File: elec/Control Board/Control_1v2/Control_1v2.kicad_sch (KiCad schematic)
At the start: 164 parts, among them J1 DB9_Female_MountingHoles, J10 Conn_02x12_Odd_Even, J11 Screw_Terminal_01x02, J14 Conn_01x10, J2 Conn_01x08, J25 Screw_Terminal_01x02, J26 Conn_01x10, J27 Conn_02x12_Odd_Even, J28 Screw_Terminal_01x02, J29 Conn_01x10, J3 Conn_01x08, J37 Conn_01x04, J4 Conn_01x08, J5 Conn_01x08, J6 Conn_01x08, J7 Conn_01x10, J8 Conn_02x18_Odd_Even, J9 Conn_01x10, Q601 BSS138

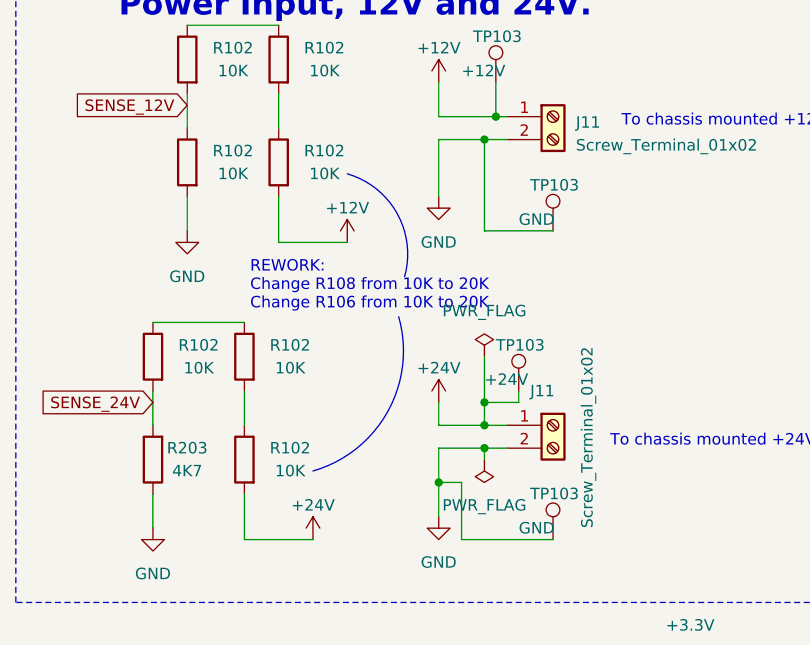
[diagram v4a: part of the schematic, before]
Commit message: Contrl 1.2 schematic, fix for Issue: not enough overhead on the 12v and 24v sense lines #145
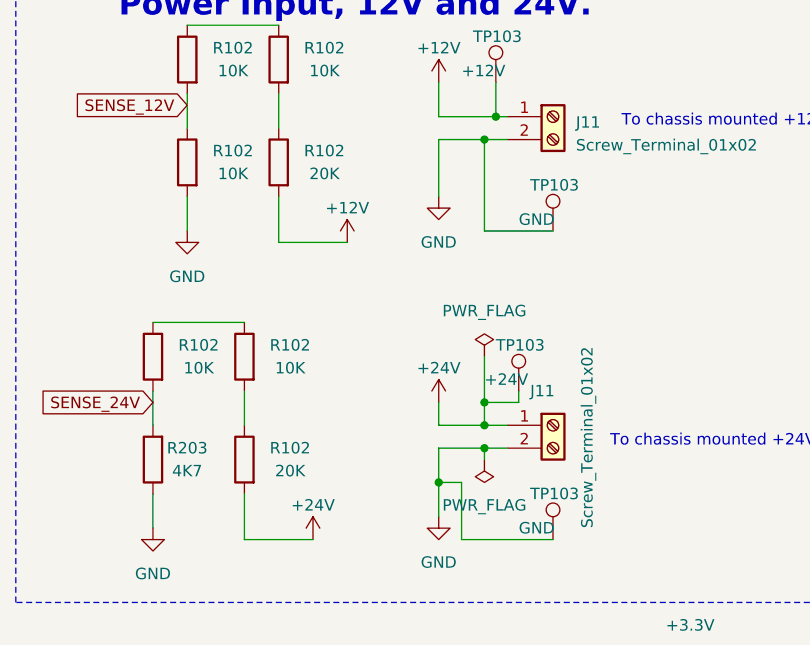
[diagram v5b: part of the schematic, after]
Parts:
- R102: value 10K -> 20K; Cost 0.0015 -> 0.0008; Distributor 1 PN C269701 -> C25804; MPN RMC060310KFN -> 0603WAF1002T5E; Manufacturer TyoHM -> UNI-ROYAL(Uniroyal Elec)
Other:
- note removed: "REWORK: Change R108 from 10K to 20K Change R106 from 10K to 20K"
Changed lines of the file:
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@@
     (stroke (width 0) (type default))
   )
-  (arc (start 459.74 178.435) (mid 465.2823 182.8401) (end 466.108 189.875)
-    (stroke (width 0) (type default))
-    (fill (type none))
-  )
   (rectangle (start 160.02 211.455) (end 259.715 272.415)
     (stroke (width 0.0762) (type dash))
@@
     (fill (type none))
   )
-  (arc (start 465.455 194.31) (mid 464.2381 204.8523) (end 455.93 211.455)
-    (stroke (width 0) (type default))
-    (fill (type none))
-  )
   (image (at 508 294.64) (scale 0.75)
     (data
@@
     (effects (font (size 1.27 1.27)) (justify left bottom))
   )
-  (text "REWORK:\nChange R108 from 10K to 20K\nChange R106 from 10K to 20K"
-    (at 448.945 193.675 0)
-    (effects (font (size 1.27 1.27)) (justify left bottom))
-  )
   (text "One Wire Thermocouple amplifiter\nDATA is bidirectional GPIO"
     (at 61.595 161.925 0)
@@
       (effects (font (size 1.27 1.27)))
     )
-    (property "Value" "10K" (at 453.39 211.455 0)
+    (property "Value" "20K" (at 453.39 211.455 0)
       (effects (font (size 1.27 1.27)))
     )
@@
       (effects (font (size 1.27 1.27)) hide)
     )
-    (property "Distributor 1 PN" "C269701" (at 448.31 210.185 90)
+    (property "Distributor 1 PN" "C25804" (at 448.31 210.185 90)
       (effects (font (size 1.27 1.27)) hide)
     )
-    (property "Manufacturer" "TyoHM" (at 448.31 210.185 90)
+    (property "Manufacturer" "UNI-ROYAL(Uniroyal Elec)" (at 448.31 210.185 90)
       (effects (font (size 1.27 1.27)) hide)
     )
-    (property "MPN" "RMC060310KFN" (at 448.31 210.185 90)
+    (property "MPN" "0603WAF1002T5E" (at 448.31 210.185 90)
       (effects (font (size 1.27 1.27)) hide)
     )
-    (property "Description" "100mW ±1% 10kΩ 0603 Chip Resistor - Surface Mount ROHS" (at 448.31 210.185 0)
+    (property "Description" "100mW Thick Film Resistors 75V ±100ppm/℃ ±1% 10kΩ 0603 Chip Resistor - Surface Mount ROHS" (at 448.31 210.185 0)
       (effects (font (size 1.27 1.27)) hide)
     )
@@
       (effects (font (size 1.27 1.27)) hide)
     )
-    (property "Cost" "0.0015" (at 448.31 210.185 0)
+    (property "Cost" "0.0008" (at 448.31 210.185 0)
       (effects (font (size 1.27 1.27)) hide)
     )
@@
       (effects (font (size 1.27 1.27)))
     )
-    (property "Value" "10K" (at 457.2 178.435 0)
+    (property "Value" "20K" (at 457.2 178.435 0)
       (effects (font (size 1.27 1.27)))
     )
@@
       (effects (font (size 1.27 1.27)) hide)
     )
-    (property "Distributor 1 PN" "C269701" (at 452.12 177.165 90)
+    (property "Distributor 1 PN" "C25804" (at 452.12 177.165 90)
       (effects (font (size 1.27 1.27)) hide)
     )
-    (property "Manufacturer" "TyoHM" (at 452.12 177.165 90)
+    (property "Manufacturer" "UNI-ROYAL(Uniroyal Elec)" (at 452.12 177.165 90)
       (effects (font (size 1.27 1.27)) hide)
     )
-    (property "MPN" "RMC060310KFN" (at 452.12 177.165 90)
+    (property "MPN" "0603WAF1002T5E" (at 452.12 177.165 90)
       (effects (font (size 1.27 1.27)) hide)
     )
-    (property "Description" "100mW ±1% 10kΩ 0603 Chip Resistor - Surface Mount ROHS" (at 452.12 177.165 0)
+    (property "Description" "100mW Thick Film Resistors 75V ±100ppm/℃ ±1% 10kΩ 0603 Chip Resistor - Surface Mount ROHS" (at 452.12 177.165 0)
       (effects (font (size 1.27 1.27)) hide)
     )
@@
       (effects (font (size 1.27 1.27)) hide)
     )
-    (property "Cost" "0.0015" (at 452.12 177.165 0)
+    (property "Cost" "0.0008" (at 452.12 177.165 0)
       (effects (font (size 1.27 1.27)) hide)
     )

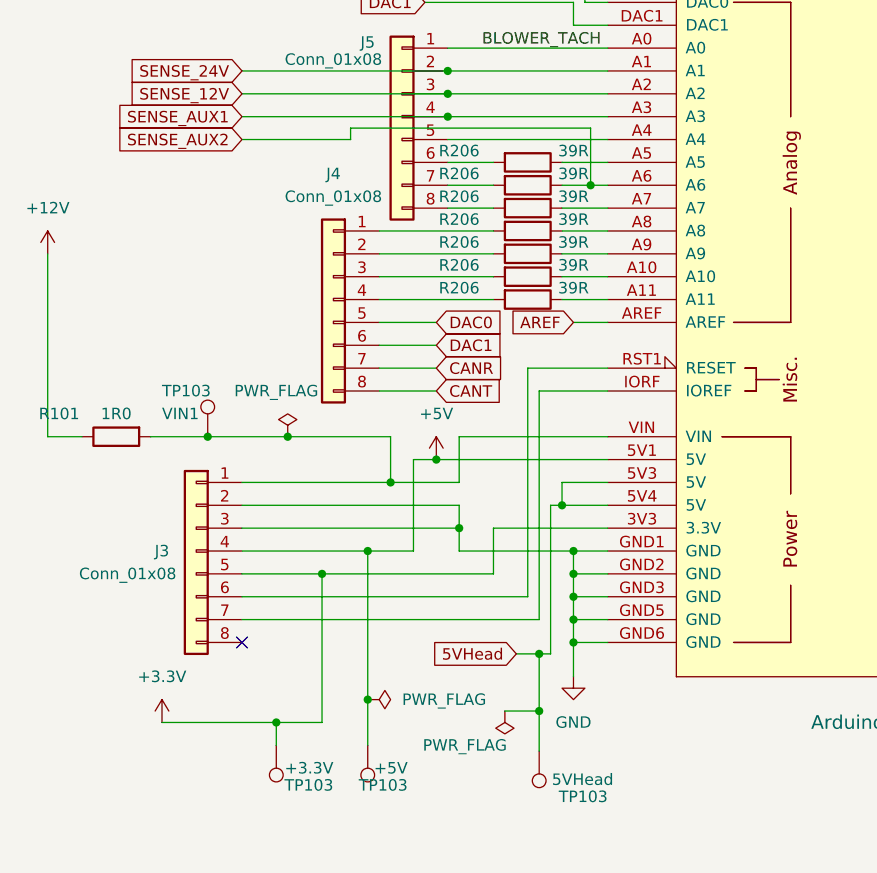
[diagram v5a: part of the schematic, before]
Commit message: Contrl 1.2 schematic, fix for Issue: Connect J3 pin 8 to the Due, Footrpint Arduino_Due_Shield_Annotated Missing Pin Number on ND on Schematic symbol and footprint. #348
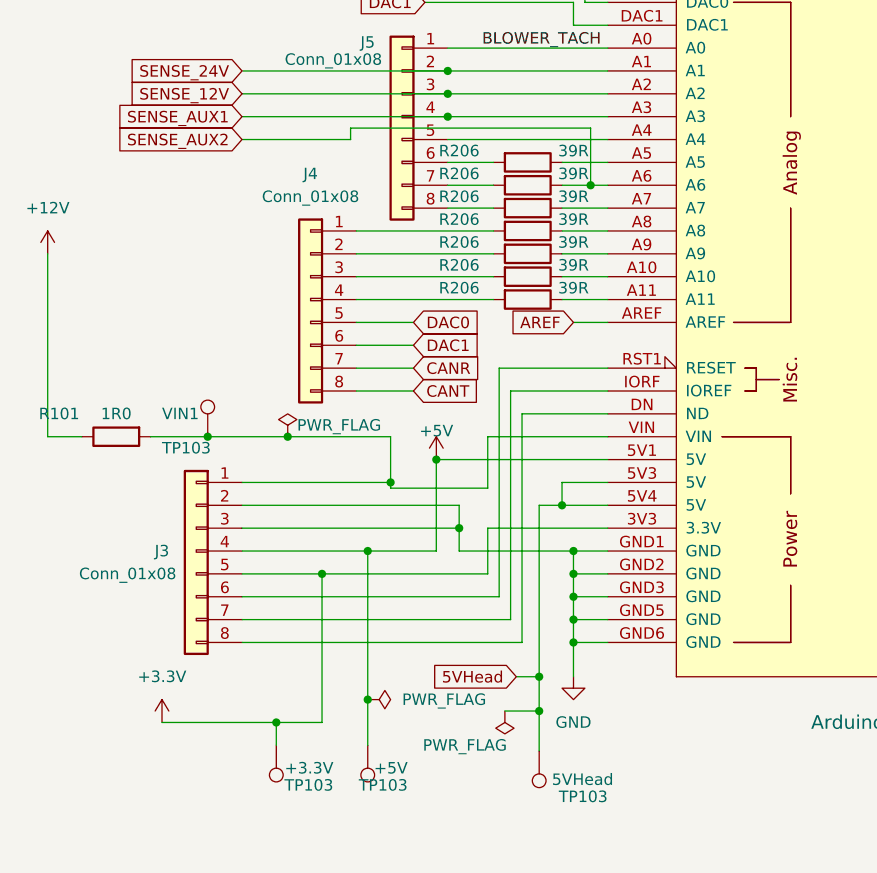
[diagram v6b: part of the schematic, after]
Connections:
- net at J3.8 (Pin_8): now also A1.DN (ND)
- no-connect marks 3 -> 2
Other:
- moved on the sheet: J4

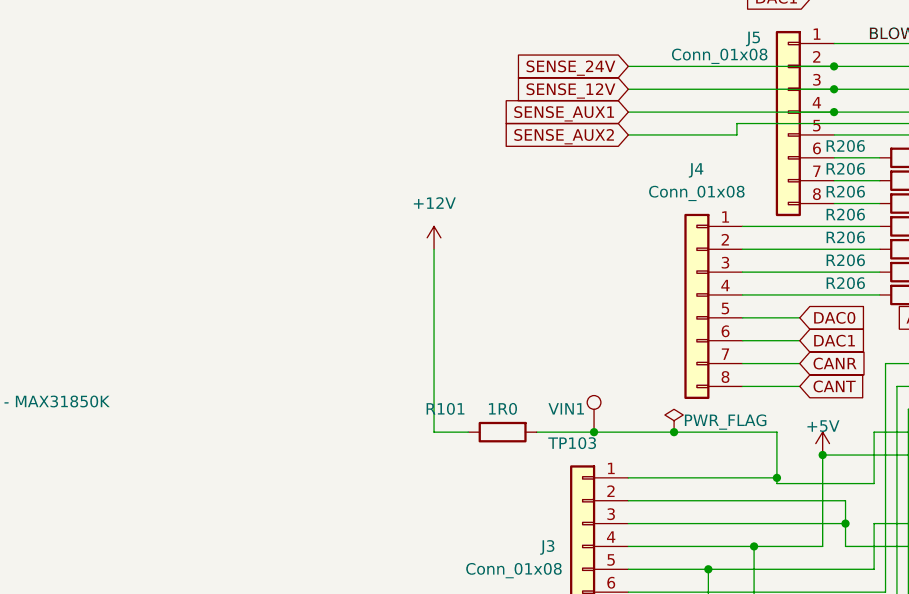
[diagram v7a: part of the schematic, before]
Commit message: Update Control_1v2.kicad_sch for Add Assembly versioning resistors #350.
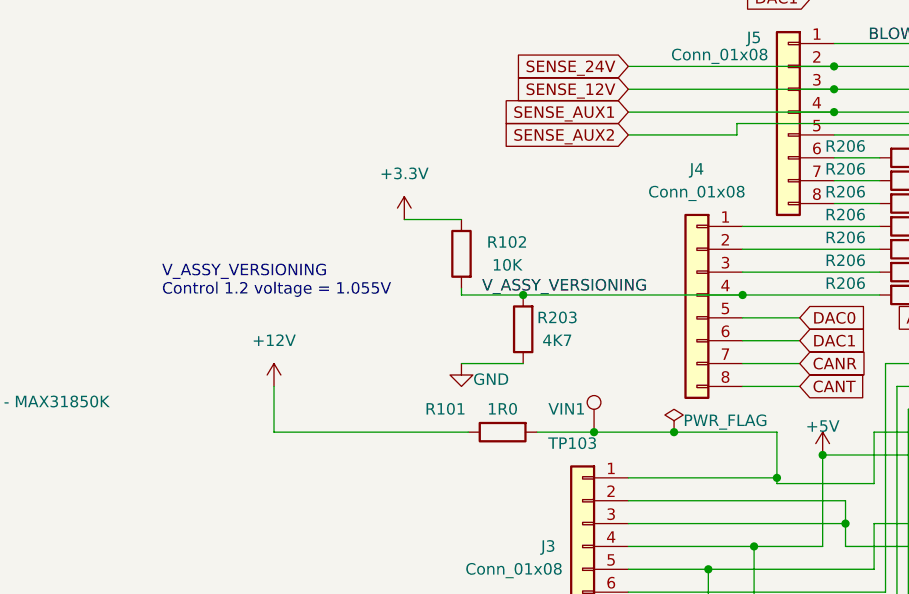
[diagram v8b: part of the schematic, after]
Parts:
- added R102: 10K, Resistor_SMD:R_0603_1608Metric_Pad0.98x0.95mm_HandSolder, symbol Device:R
- added R203: 4K7, Resistor_SMD:R_0603_1608Metric_Pad0.98x0.95mm_HandSolder, symbol Device:R
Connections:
- net +3.3V: now also R102.1
- net GND: now also R203.1
- net V_ASSY_VERSIONING: now reaches J4.4 (Pin_4), R206.2
- net V_ASSY_VERSIONING: now also R102.2, R203.2
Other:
- note added: "V_ASSY_VERSIONING Control 1.2 voltage = 1.055V"
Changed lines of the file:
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@@
   (junction (at 214.63 234.95) (diameter 0) (color 0 0 0 0)
   )
+  (junction (at 164.846 137.16) (diameter 0) (color 0 0 0 0)
+  )
   (junction (at 269.24 204.47) (diameter 0) (color 0 0 0 0)
   )
@@
   (junction (at 64.77 44.45) (diameter 0) (color 0 0 0 0)
   )
+  (junction (at 189.23 137.16) (diameter 0) (color 0 0 0 0)
+  )
   (junction (at 213.36 175.26) (diameter 0) (color 0 0 0 0)
   )
@@
     (stroke (width 0) (type default))
   )
+  (wire (pts (xy 164.846 137.16) (xy 189.23 137.16))
+    (stroke (width 0) (type default))
+  )
   (wire (pts (xy 443.23 60.96) (xy 433.07 60.96))
     (stroke (width 0) (type default))
@@
     (stroke (width 0) (type default))
   )
+  (wire (pts (xy 151.638 128.778) (xy 157.988 128.778))
+    (stroke (width 0) (type default))
+  )
   (wire (pts (xy 203.2 49.53) (xy 203.2 46.99))
     (stroke (width 0) (type default))
@@
     (stroke (width 0) (type default))
   )
+  (wire (pts (xy 189.23 137.16) (xy 204.47 137.16))
+    (stroke (width 0) (type default))
+  )
   (wire (pts (xy 172.72 152.4) (xy 181.61 152.4))
     (stroke (width 0) (type default))
@@
     (stroke (width 0) (type default))
   )
+  (wire (pts (xy 157.988 137.16) (xy 164.846 137.16))
+    (stroke (width 0) (type default))
+  )
   (wire (pts (xy 273.05 199.39) (xy 269.24 199.39))
     (stroke (width 0) (type default))
@@
     (stroke (width 0) (type default))
   )
+  (wire (pts (xy 157.988 136.398) (xy 157.988 137.16))
+    (stroke (width 0) (type default))
+  )
   (wire (pts (xy 359.41 162.56) (xy 359.41 175.26))
     (stroke (width 0) (type default))
@@
     (stroke (width 0) (type default))
   )
-  (wire (pts (xy 189.23 137.16) (xy 204.47 137.16))
-    (stroke (width 0) (type default))
-  )
   (wire (pts (xy 203.2 46.99) (xy 215.9 46.99))
     (stroke (width 0) (type default))
@@
     (stroke (width 0) (type default))
   )
+  (wire (pts (xy 157.988 144.78) (xy 164.846 144.78))
+    (stroke (width 0) (type default))
+  )
   (wire (pts (xy 477.52 58.42) (xy 455.93 58.42))
     (stroke (width 0) (type default))
@@
     (stroke (width 0) (type default))
   )
-  (wire (pts (xy 154.94 132.08) (xy 154.94 152.4))
+  (wire (pts (xy 137.16 147.32) (xy 137.16 152.4))
     (stroke (width 0) (type default))
   )
@@
     (stroke (width 0) (type default))
   )
-  (wire (pts (xy 154.94 152.4) (xy 158.75 152.4))
+  (wire (pts (xy 137.16 152.4) (xy 158.75 152.4))
     (stroke (width 0) (type default))
   )
@@
     (effects (font (size 2.54 2.54)) (justify left bottom))
   )
+  (text "V_ASSY_VERSIONING\nControl 1.2 voltage = 1.055V" (at 124.714 137.414 0)
+    (effects (font (size 1.27 1.27)) (justify left bottom))
+  )
   (text "Heart beat, \nLoop OK" (at 364.49 87.63 0)
     (effects (font (size 1.27 1.27)) (justify left bottom))
@@
     (effects (font (size 1.27 1.27)) (justify right bottom))
   )
+  (label "V_ASSY_VERSIONING" (at 160.274 137.16 0) (fields_autoplaced)
+    (effects (font (size 1.27 1.27)) (justify left bottom))
+  )
   (label "GND" (at 439.42 66.04 180) (fields_autoplaced)
     (effects (font (size 1.27 1.27)) (justify right bottom))
@@
     )
   )
+  (symbol (lib_id "power:+3.3V") (at 151.638 128.778 0) (mirror y) (unit 1)
+    (in_bom yes) (on_board yes) (dnp no) (fields_autoplaced)
+    (property "Reference" "#PWR064" (at 151.638 132.588 0)
+      (effects (font (size 1.27 1.27)) hide)
+    )
+    (property "Value" "+3.3V" (at 151.638 123.698 0)
+      (effects (font (size 1.27 1.27)))
+    )
+    (property "Footprint" "" (at 151.638 128.778 0)
+      (effects (font (size 1.27 1.27)) hide)
+    )
+    (property "Datasheet" "" (at 151.638 128.778 0)
+      (effects (font (size 1.27 1.27)) hide)
+    )
+    (pin "1")
+    (instances
+      (project "Control_1v2"
+        (path "/c68c9deb-8d4d-42f0-adf8-4d3022f4ee59"
+          (reference "#PWR064") (unit 1)
+        )
+      )
+    )
+  )
   (symbol (lib_id "Device:R") (at 444.5 246.38 270) (unit 1)
     (in_bom yes) (on_board yes) (dnp no)
@@
     )
   )
+  (symbol (lib_id "Device:R") (at 164.846 140.97 180) (unit 1)
+    (in_bom yes) (on_board yes) (dnp no)
+    (property "Reference" "R203" (at 168.656 139.7 0)
+      (effects (font (size 1.27 1.27)))
+    )
+    (property "Value" "4K7" (at 168.656 142.24 0)
+      (effects (font (size 1.27 1.27)))
+    )
+    (property "Footprint" "Resistor_SMD:R_0603_1608Metric_Pad0.98x0.95mm_HandSolder" (at 166.624 140.97 90)
+      (effects (font (size 1.27 1.27)) hide)
+    )
+    (property "Datasheet" "~" (at 164.846 140.97 0)
+      (effects (font (size 1.27 1.27)) hide)
+    )
+    (property "Distributor 1" "JLCPCB" (at 164.846 140.97 90)
+      (effects (font (size 1.27 1.27)) hide)
+    )
+    (property "Distributor 1 PN" "C23162" (at 164.846 140.97 90)
+      (effects (font (size 1.27 1.27)) hide)
+    )
+    (property "Manufacturer" "UNI-ROYAL(Uniroyal Elec)" (at 164.846 140.97 90)
+      (effects (font (size 1.27 1.27)) hide)
+    )
+    (property "MPN" "RMC 0603 4K7 F N" (at 164.846 140.97 90)
+      (effects (font (size 1.27 1.27)) hide)
+    )
+    (property "Description" "100mW Thick Film Resistors ±100ppm/℃ ±1% 4.7kΩ 0603 Chip Resistor - Surface Mount ROHS" (at 164.846 140.97 0)
+      (effects (font (size 1.27 1.27)) hide)
+    )
+    (property "AssemblyType" "SMT" (at 164.846 140.97 0)
+      (effects (font (size 1.27 1.27)) hide)
+    )
+    (property "Cost" "0.0015" (at 164.846 140.97 0)
+      (effects (font (size 1.27 1.27)) hide)
+    )
+    (pin "1")
+    (pin "2")
+    (instances
+      (project "GeneralPurposeAlarmDevicePCB"
+        (path "/412a327d-1ee3-473e-bc00-1545004b7edf/00000000-0000-0000-0000-000062b3ac2f"
+          (reference "R203") (unit 1)
+        )
+      )
+      (project "Control_1v2"
+        (path "/c68c9deb-8d4d-42f0-adf8-4d3022f4ee59"
+          (reference "R?") (unit 1)
+        )
+      )
+    )
+  )
   (symbol (lib_id "Device:R") (at 497.84 256.54 270) (unit 1)
     (in_bom yes) (on_board yes) (dnp no)
@@
     )
   )
-  (symbol (lib_id "power:+12V") (at 154.94 132.08 0) (unit 1)
+  (symbol (lib_id "power:+12V") (at 137.16 147.32 0) (unit 1)
     (in_bom yes) (on_board yes) (dnp no)
-    (property "Reference" "#PWR014" (at 154.94 135.89 0)
+    (property "Reference" "#PWR014" (at 137.16 151.13 0)
       (effects (font (size 1.27 1.27)) hide)
     )
-    (property "Value" "+12V" (at 154.94 127 0)
+    (property "Value" "+12V" (at 137.16 142.24 0)
       (effects (font (size 1.27 1.27)))
     )
-    (property "Footprint" "" (at 154.94 132.08 0)
+    (property "Footprint" "" (at 137.16 147.32 0)
       (effects (font (size 1.27 1.27)) hide)
     )
-    (property "Datasheet" "" (at 154.94 132.08 0)
+    (property "Datasheet" "" (at 137.16 147.32 0)
       (effects (font (size 1.27 1.27)) hide)
     )
@@
     )
   )
+  (symbol (lib_id "power:GND") (at 157.988 144.78 0) (unit 1)
+    (in_bom yes) (on_board yes) (dnp no)
+    (property "Reference" "#PWR0108" (at 157.988 151.13 0)
+      (effects (font (size 1.27 1.27)) hide)
+    )
+    (property "Value" "GND" (at 161.29 146.558 0)
+      (effects (font (size 1.27 1.27)))
+    )
+    (property "Footprint" "" (at 157.988 144.78 0)
+      (effects (font (size 1.27 1.27)) hide)
+    )
+    (property "Datasheet" "" (at 157.988 144.78 0)
+      (effects (font (size 1.27 1.27)) hide)
+    )
+    (pin "1")
+    (instances
+      (project "Control_1v2"
+        (path "/c68c9deb-8d4d-42f0-adf8-4d3022f4ee59"
+          (reference "#PWR0108") (unit 1)
+        )
+      )
+    )
+  )
   (symbol (lib_id "Device:R") (at 56.515 301.625 90) (mirror x) (unit 1)
     (in_bom yes) (on_board yes) (dnp no)
@@
         )
       )
+    )
+  )
+  (symbol (lib_id "Device:R") (at 157.988 132.588 0) (mirror y) (unit 1)
+    (in_bom yes) (on_board yes) (dnp no)
+    (property "Reference" "R102" (at 163.068 131.318 0)
+      (effects (font (size 1.27 1.27)))
+    )
+    (property "Value" "10K" (at 163.068 133.858 0)
+      (effects (font (size 1.27 1.27)))
+    )
+    (property "Footprint" "Resistor_SMD:R_0603_1608Metric_Pad0.98x0.95mm_HandSolder" (at 159.766 132.588 90)
+      (effects (font (size 1.27 1.27)) hide)
+    )
+    (property "Datasheet" "https://datasheet.lcsc.com/lcsc/1811101310_TyoHM-RMC06031K1-N_C269704.pdf" (at 157.988 132.588 0)
+      (effects (font (size 1.27 1.27)) hide)
+    )
+    (property "Distributor 1" "JLCPCB" (at 157.988 132.588 90)
+      (effects (font (size 1.27 1.27)) hide)
+    )
+    (property "Distributor 1 PN" "C269701" (at 157.988 132.588 90)
+      (effects (font (size 1.27 1.27)) hide)
+    )
+    (property "Manufacturer" "TyoHM" (at 157.988 132.588 90)
+      (effects (font (size 1.27 1.27)) hide)
+    )
+    (property "MPN" "RMC060310KFN" (at 157.988 132.588 90)
+      (effects (font (size 1.27 1.27)) hide)
+    )
+    (property "Description" "100mW ±1% 10kΩ 0603 Chip Resistor - Surface Mount ROHS" (at 157.988 132.588 0)
+      (effects (font (size 1.27 1.27)) hide)
+    )
+    (property "AssemblyType" "SMT" (at 157.988 132.588 0)
+      (effects (font (size 1.27 1.27)) hide)
+    )
+    (property "Cost" "0.0015" (at 157.988 132.588 0)
+      (effects (font (size 1.27 1.27)) hide)
+    )
+    (property "LongLead" "NO" (at 157.988 132.588 0)
+      (effects (font (size 1.27 1.27)) hide)
+    )
+    (pin "1")
+    (pin "2")
+    (instances
+      (project "GeneralPurposeAlarmDevicePCB"
+        (path "/412a327d-1ee3-473e-bc00-1545004b7edf"
+          (reference "R102") (unit 1)
+        )
+      )
+      (project "Control_1v2"
+        (path "/c68c9deb-8d4d-42f0-adf8-4d3022f4ee59/0cb2f0dc-fe38-451d-b752-5d12a98f8d03"
+          (reference "R44") (unit 1)
+        )
+        (path "/c68c9deb-8d4d-42f0-adf8-4d3022f4ee59"
+          (reference "R?") (unit 1)
+        )
+      )
